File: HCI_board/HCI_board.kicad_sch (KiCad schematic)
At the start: 27 parts, among them J1 MCU Controls, J3 Power, J7 DC Motor Terminal, J9 USBC_RECP, SW1 Trigger, SW2 Increment, SW3 Reset, SW4 Decrement, U1 NCP1117, U3 DRV8833PWP

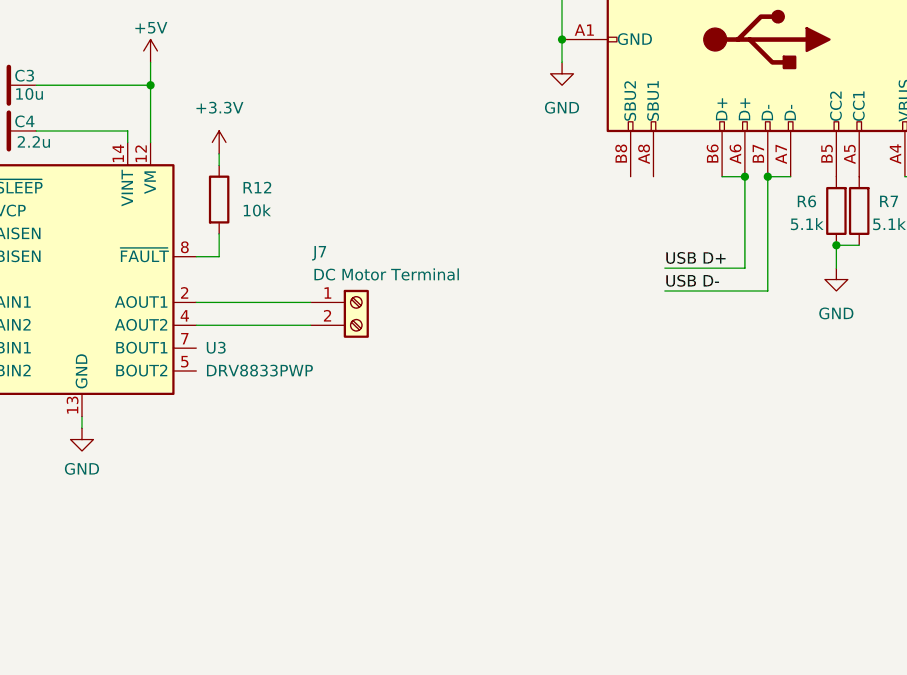
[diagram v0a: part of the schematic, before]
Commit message: Addeed indicator LEDs
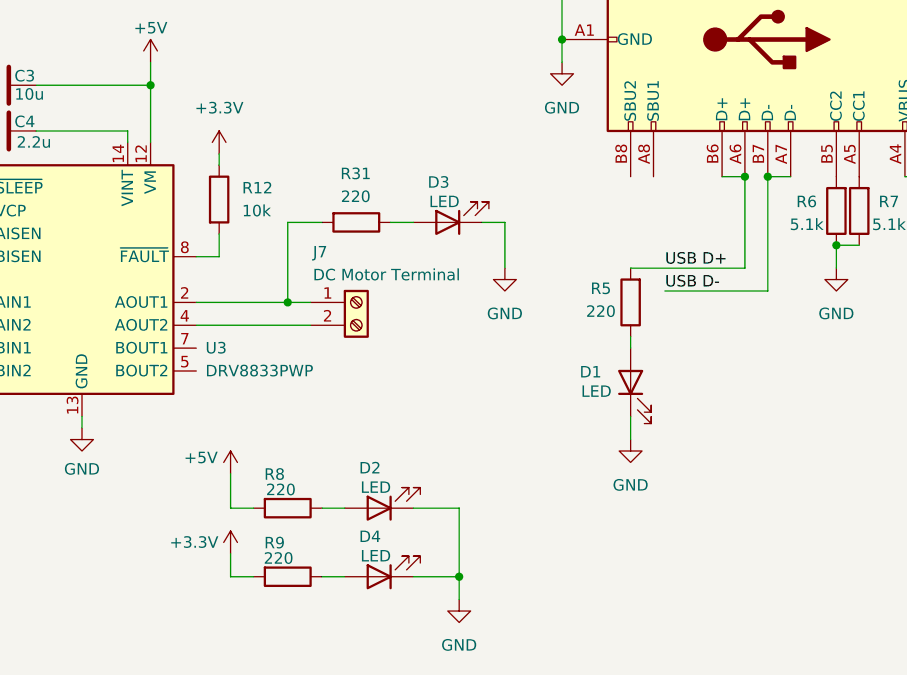
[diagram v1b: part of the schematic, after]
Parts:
- added D1, D2, D3, D4: LED, LED_SMD:LED_0402_1005Metric, symbol Device:LED
- added R31, R5, R8, R9: 220, Resistor_SMD:R_0402_1005Metric, symbol Device:R
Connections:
- net +3.3V: now also R9.2
- net +5V: now also R8.2
- net GND: now also D1.1 (K), D2.1 (K), D3.1 (K), D4.1 (K)
- net USB D+: now also R5.2
- net at J7.1 (Pin_1), U3.2 (AOUT1): now also R31.2
- new net: D3.2 (A), R31.1
- new net: D4.2 (A), R9.1
- new net: D2.2 (A), R8.1
- new net: D1.2 (A), R5.1
